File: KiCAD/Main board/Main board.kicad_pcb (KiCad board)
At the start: 2 copper layers, 190 x 125 mm, 123 parts, among them J1 Conn_01x03, J10 Conn_01x03, J11 Conn_01x03, J12 Conn_01x03, J2 Conn_01x03, J3 Conn_01x02, J4 Conn_01x02, J5 Conn_01x03, J6 Conn_01x02, J7 Conn_01x03, J8 Conn_01x02, J9 Conn_01x03, U1 PCM1789, U12 LIN_REG_±5V, U13 LIN_REG_±5V, U14 LIN_REG_±12V, U15 LIN_REG_±12V, U18 12V, U19 5V, U2 LM4562, U20 8V, U21 15V, U3 OPA1632DR, U4 OPA1632DR, U5 OPA1632DR, U7 PCM1804, U9 SEPIC_-15V_LT3579

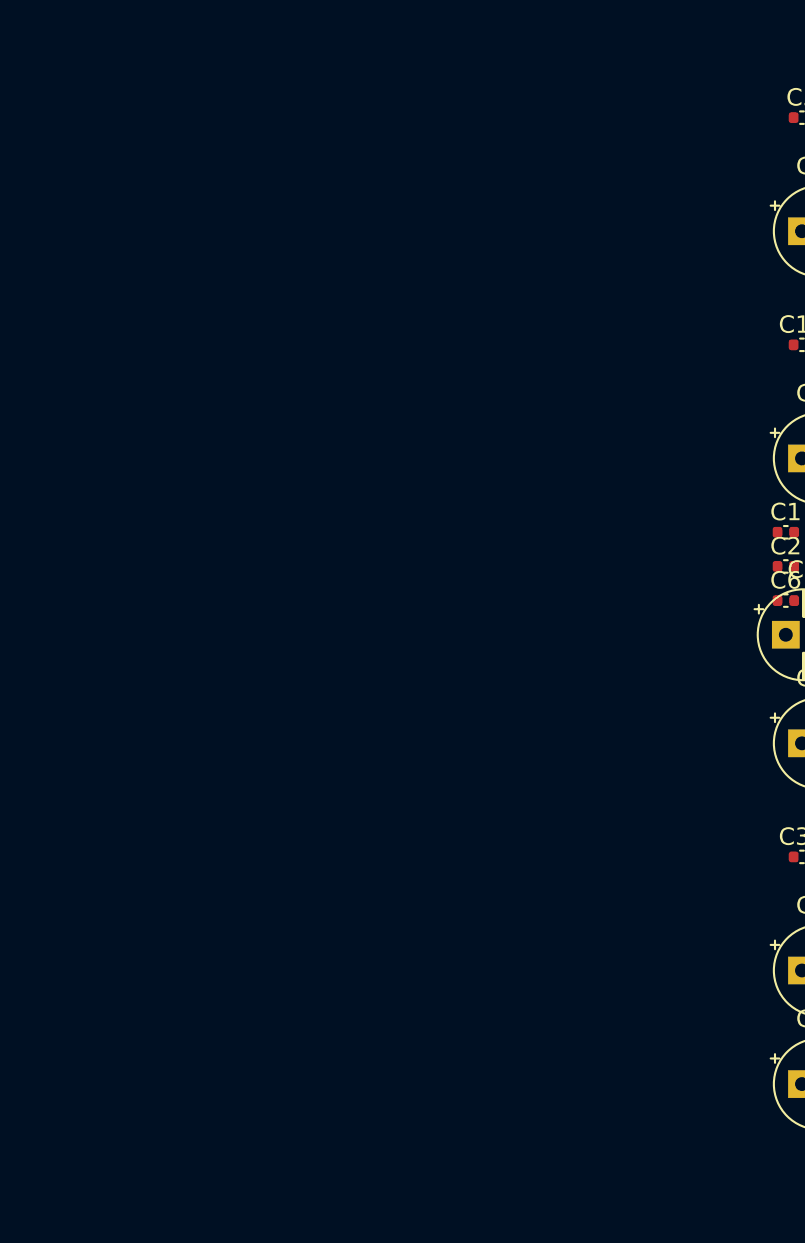
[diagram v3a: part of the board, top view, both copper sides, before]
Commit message: Worked on SDD, main board schematic and LTspice discrete linear regulator
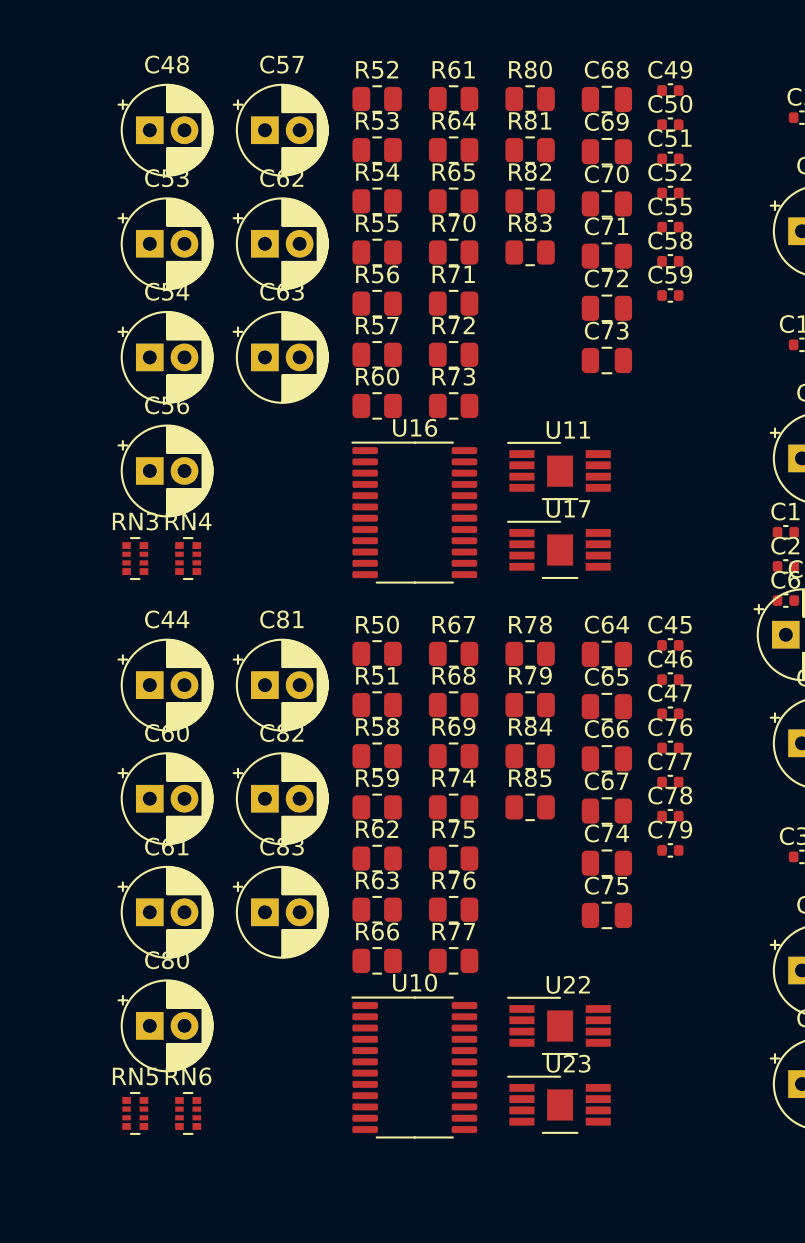
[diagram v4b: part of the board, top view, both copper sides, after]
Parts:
- added C44: 22uF, Capacitor_THT:CP_Radial_D5.0mm_P2.00mm, F.Cu at (278.1, 71.8)
- added C45: 100n, Capacitor_SMD:C_0402_1005Metric, F.Cu at (308.2, 69.5)
- added C46: 100n, Capacitor_SMD:C_0402_1005Metric, F.Cu at (308.2, 71.5)
- added C47: 100n, Capacitor_SMD:C_0402_1005Metric, F.Cu at (308.2, 73.5)
- added C48: 22uF, Capacitor_THT:CP_Radial_D5.0mm_P2.00mm, F.Cu at (278.1, 39.8)
- added C49: 100n, Capacitor_SMD:C_0402_1005Metric, F.Cu at (308.2, 37.5)
- added C50: 100n, Capacitor_SMD:C_0402_1005Metric, F.Cu at (308.2, 39.5)
- added C51: 100n, Capacitor_SMD:C_0402_1005Metric, F.Cu at (308.2, 41.5)
- added C52: 100n, Capacitor_SMD:C_0402_1005Metric, F.Cu at (308.2, 43.4)
- added C53: 22uF, Capacitor_THT:CP_Radial_D5.0mm_P2.00mm, F.Cu at (278.1, 46.4)
- added C54: 22uF, Capacitor_THT:CP_Radial_D5.0mm_P2.00mm, F.Cu at (278.1, 52.9)
- added C55: 100n, Capacitor_SMD:C_0402_1005Metric, F.Cu at (308.2, 45.4)
- added C56: 22uF, Capacitor_THT:CP_Radial_D5.0mm_P2.00mm, F.Cu at (278.1, 59.5)
- added C57: 22uF, Capacitor_THT:CP_Radial_D5.0mm_P2.00mm, F.Cu at (284.8, 39.8)
- added C58: 100n, Capacitor_SMD:C_0402_1005Metric, F.Cu at (308.2, 47.4)
- added C59: 100n, Capacitor_SMD:C_0402_1005Metric, F.Cu at (308.2, 49.4)
- added C60: 22uF, Capacitor_THT:CP_Radial_D5.0mm_P2.00mm, F.Cu at (278.1, 78.4)
- added C61: 22uF, Capacitor_THT:CP_Radial_D5.0mm_P2.00mm, F.Cu at (278.1, 84.9)
- added C62: 22uF, Capacitor_THT:CP_Radial_D5.0mm_P2.00mm, F.Cu at (284.8, 46.4)
- added C63: 22uF, Capacitor_THT:CP_Radial_D5.0mm_P2.00mm, F.Cu at (284.8, 52.9)
- added C64: 680p, Capacitor_SMD:C_0805_2012Metric, F.Cu at (304.5, 70.1)
- added C65: 680, Capacitor_SMD:C_0805_2012Metric, F.Cu at (304.5, 73.1)
- added C66: 680p, Capacitor_SMD:C_0805_2012Metric, F.Cu at (304.5, 76.1)
- added C67: 680, Capacitor_SMD:C_0805_2012Metric, F.Cu at (304.5, 79.1)
- added C68: 680p, Capacitor_SMD:C_0805_2012Metric, F.Cu at (304.5, 38.1)
- added C69: 680, Capacitor_SMD:C_0805_2012Metric, F.Cu at (304.5, 41.1)
- added C70: 680p, Capacitor_SMD:C_0805_2012Metric, F.Cu at (304.5, 44.1)
- added C71: 680, Capacitor_SMD:C_0805_2012Metric, F.Cu at (304.5, 47.1)
- added C72: 2n2, Capacitor_SMD:C_0805_2012Metric, F.Cu at (304.5, 50.1)
- added C73: 2n2, Capacitor_SMD:C_0805_2012Metric, F.Cu at (304.5, 53.1)
- added C74: 2n2, Capacitor_SMD:C_0805_2012Metric, F.Cu at (304.5, 82.1)
- added C75: 2n2, Capacitor_SMD:C_0805_2012Metric, F.Cu at (304.5, 85.1)
- added C76: 100n, Capacitor_SMD:C_0402_1005Metric, F.Cu at (308.2, 75.4)
- added C77: 100n, Capacitor_SMD:C_0402_1005Metric, F.Cu at (308.2, 77.4)
- added C78: 100n, Capacitor_SMD:C_0402_1005Metric, F.Cu at (308.2, 79.4)
- added C79: 100n, Capacitor_SMD:C_0402_1005Metric, F.Cu at (308.2, 81.4)
- added C80: 22uF, Capacitor_THT:CP_Radial_D5.0mm_P2.00mm, F.Cu at (278.1, 91.5)
- added C81: 22uF, Capacitor_THT:CP_Radial_D5.0mm_P2.00mm, F.Cu at (284.8, 71.8)
- added C82: 22uF, Capacitor_THT:CP_Radial_D5.0mm_P2.00mm, F.Cu at (284.8, 78.4)
- added C83: 22uF, Capacitor_THT:CP_Radial_D5.0mm_P2.00mm, F.Cu at (284.8, 84.9)
- added R50: 10R, Resistor_SMD:R_0805_2012Metric, F.Cu at (291.2, 70.0)
- added R51: 10R, Resistor_SMD:R_0805_2012Metric, F.Cu at (291.2, 73.0)
- added R52: 10R, Resistor_SMD:R_0805_2012Metric, F.Cu at (291.2, 38.0)
- added R53: 10R, Resistor_SMD:R_0805_2012Metric, F.Cu at (291.2, 41.0)
- added R54: 10R, Resistor_SMD:R_0805_2012Metric, F.Cu at (291.2, 43.9)
- added R55: 10R, Resistor_SMD:R_0805_2012Metric, F.Cu at (291.2, 46.9)
- added R56: 10R, Resistor_SMD:R_0805_2012Metric, F.Cu at (291.2, 49.8)
- added R57: 10R, Resistor_SMD:R_0805_2012Metric, F.Cu at (291.2, 52.8)
- added R58: 1k, Resistor_SMD:R_0805_2012Metric, F.Cu at (291.2, 75.9)
- added R59: 1k, Resistor_SMD:R_0805_2012Metric, F.Cu at (291.2, 78.9)
- added R60: 1k, Resistor_SMD:R_0805_2012Metric, F.Cu at (291.2, 55.7)
- added R61: 1k, Resistor_SMD:R_0805_2012Metric, F.Cu at (295.7, 38.0)
- added R62: 1k, Resistor_SMD:R_0805_2012Metric, F.Cu at (291.2, 81.8)
- added R63: 1k, Resistor_SMD:R_0805_2012Metric, F.Cu at (291.2, 84.8)
- added R64: 1k, Resistor_SMD:R_0805_2012Metric, F.Cu at (295.7, 41.0)
- added R65: 1k, Resistor_SMD:R_0805_2012Metric, F.Cu at (295.7, 43.9)
- added R66: 4k7, Resistor_SMD:R_0805_2012Metric, F.Cu at (291.2, 87.7)
- added R67: 4k7, Resistor_SMD:R_0805_2012Metric, F.Cu at (295.7, 70.0)
- added R68: 4k7, Resistor_SMD:R_0805_2012Metric, F.Cu at (295.7, 73.0)
- added R69: 4k7, Resistor_SMD:R_0805_2012Metric, F.Cu at (295.7, 75.9)
- added R70: 4k7, Resistor_SMD:R_0805_2012Metric, F.Cu at (295.7, 46.9)
- added R71: 4k7, Resistor_SMD:R_0805_2012Metric, F.Cu at (295.7, 49.8)
- added R72: 4k7, Resistor_SMD:R_0805_2012Metric, F.Cu at (295.7, 52.8)
- added R73: 4k7, Resistor_SMD:R_0805_2012Metric, F.Cu at (295.7, 55.7)
- added R74: 39, Resistor_SMD:R_0805_2012Metric, F.Cu at (295.7, 78.9)
- added R75: 39, Resistor_SMD:R_0805_2012Metric, F.Cu at (295.7, 81.8)
- added R76: 39, Resistor_SMD:R_0805_2012Metric, F.Cu at (295.7, 84.8)
- added R77: 39, Resistor_SMD:R_0805_2012Metric, F.Cu at (295.7, 87.7)
- added R78: 10R, Resistor_SMD:R_0805_2012Metric, F.Cu at (300.1, 70.0)
- added R79: 10R, Resistor_SMD:R_0805_2012Metric, F.Cu at (300.1, 73.0)
- added R80: 39, Resistor_SMD:R_0805_2012Metric, F.Cu at (300.1, 38.0)
- added R81: 39, Resistor_SMD:R_0805_2012Metric, F.Cu at (300.1, 41.0)
- added R82: 39, Resistor_SMD:R_0805_2012Metric, F.Cu at (300.1, 43.9)
- added R83: 39, Resistor_SMD:R_0805_2012Metric, F.Cu at (300.1, 46.9)
- added R84: 10R, Resistor_SMD:R_0805_2012Metric, F.Cu at (300.1, 75.9)
- added R85: 10R, Resistor_SMD:R_0805_2012Metric, F.Cu at (300.1, 78.9)
- added RN3: 22R, Resistor_SMD:R_Array_Convex_4x0402, F.Cu at (277.3, 64.5)
- added RN4: 22R, Resistor_SMD:R_Array_Convex_4x0402, F.Cu at (280.4, 64.5)
- added RN5: 22R, Resistor_SMD:R_Array_Convex_4x0402, F.Cu at (277.3, 96.5)
- added RN6: 22R, Resistor_SMD:R_Array_Convex_4x0402, F.Cu at (280.4, 96.5)
- added U10: PCM1789, Package_SO:TSSOP-24_4.4x7.8mm_P0.65mm, F.Cu at (293.4, 93.9)
- added U11: OPA1632DR, Audio-DSP:VSSOP-8_3.0x3.0mm_P0.65_TP1.8x1.5, F.Cu at (301.8, 59.5)
- added U16: PCM1789, Package_SO:TSSOP-24_4.4x7.8mm_P0.65mm, F.Cu at (293.4, 61.9)
- added U17: OPA1632DR, Audio-DSP:VSSOP-8_3.0x3.0mm_P0.65_TP1.8x1.5, F.Cu at (301.8, 64.0)
- added U22: OPA1632DR, Audio-DSP:VSSOP-8_3.0x3.0mm_P0.65_TP1.8x1.5, F.Cu at (301.8, 91.5)
- added U23: OPA1632DR, Audio-DSP:VSSOP-8_3.0x3.0mm_P0.65_TP1.8x1.5, F.Cu at (301.8, 96.0)

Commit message: Worked on main board schematic and PCB, added symbols to symbol library
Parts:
- added C100: 100n, Capacitor_SMD:C_0402_1005Metric, F.Cu at (316.1, 59.1)
- added C101: 100n, Capacitor_SMD:C_0402_1005Metric, F.Cu at (319.0, 53.2)
- added C102: 22uF, Capacitor_THT:CP_Radial_D5.0mm_P2.00mm, F.Cu at (291.8, 54.5)
- added C103: 22uF, Capacitor_THT:CP_Radial_D5.0mm_P2.00mm, F.Cu at (291.8, 61.0)
- added C104: 100n, Capacitor_SMD:C_0402_1005Metric, F.Cu at (319.0, 55.2)
- added C105: 3n3, Capacitor_SMD:C_0805_2012Metric, F.Cu at (298.3, 45.1)
- added C106: 1n, Capacitor_SMD:C_0805_2012Metric, F.Cu at (298.3, 48.1)
- added C107: 1n, Capacitor_SMD:C_0805_2012Metric, F.Cu at (298.3, 51.1)
- added C108: 2n7, Capacitor_SMD:C_0805_2012Metric, F.Cu at (298.3, 54.1)
- added C109: 100n, Capacitor_SMD:C_0402_1005Metric, F.Cu at (319.0, 57.1)
- added C110: 100n, Capacitor_SMD:C_0402_1005Metric, F.Cu at (331.9, 56.1)
- added C111: 100n, Capacitor_SMD:C_0402_1005Metric, F.Cu at (319.0, 59.1)
- added C112: 1u, Capacitor_SMD:C_0402_1005Metric, F.Cu at (296.4, 126.1)
- added C113: 1u, Capacitor_SMD:C_0402_1005Metric, F.Cu at (296.4, 128.1)
- added C114: 1u, Capacitor_SMD:C_0402_1005Metric, F.Cu at (296.4, 130.0)
- added C115: 3n3, Capacitor_SMD:C_0805_2012Metric, F.Cu at (346.7, 52.4)
- added C116: 3n3, Capacitor_SMD:C_0805_2012Metric, F.Cu at (346.7, 55.4)
- added C117: 1n, Capacitor_SMD:C_0805_2012Metric, F.Cu at (346.7, 58.4)
- added C118: 1n, Capacitor_SMD:C_0805_2012Metric, F.Cu at (346.7, 61.5)
- added C119: 2n7, Capacitor_SMD:C_0805_2012Metric, F.Cu at (346.7, 64.5)
- added C120: 100n, Capacitor_SMD:C_0402_1005Metric, F.Cu at (331.9, 58.1)
- added C35: 1n, Capacitor_SMD:C_0805_2012Metric, F.Cu at (298.3, 33.1)
- added C40: 1n, Capacitor_SMD:C_0805_2012Metric, F.Cu at (298.3, 36.1)
- added C84: 100n, Capacitor_SMD:C_0402_1005Metric, F.Cu at (313.2, 55.2)
- added C85: 1u, Capacitor_SMD:C_0402_1005Metric, F.Cu at (296.4, 124.1)
- added C86: 100n, Capacitor_SMD:C_0402_1005Metric, F.Cu at (313.2, 57.1)
- added C87: 100n, Capacitor_SMD:C_0402_1005Metric, F.Cu at (313.2, 59.1)
- added C88: 100n, Capacitor_SMD:C_0402_1005Metric, F.Cu at (316.1, 53.2)
- added C89: 22uF, Capacitor_THT:CP_Radial_D5.0mm_P2.00mm, F.Cu at (291.8, 34.8)
- added C90: 3n3, Capacitor_SMD:C_0805_2012Metric, F.Cu at (298.3, 42.1)
- added C91: 100n, Capacitor_SMD:C_0402_1005Metric, F.Cu at (316.1, 55.2)
- added C92: 3n3, Capacitor_SMD:C_0805_2012Metric, F.Cu at (342.3, 52.4)
- added C93: 3n3, Capacitor_SMD:C_0805_2012Metric, F.Cu at (342.3, 55.4)
- added C94: 1n, Capacitor_SMD:C_0805_2012Metric, F.Cu at (342.3, 58.4)
- added C95: 1n, Capacitor_SMD:C_0805_2012Metric, F.Cu at (342.3, 61.5)
- added C96: 2n7, Capacitor_SMD:C_0805_2012Metric, F.Cu at (342.3, 64.5)
- added C97: 100n, Capacitor_SMD:C_0402_1005Metric, F.Cu at (316.1, 57.1)
- added C98: 22uF, Capacitor_THT:CP_Radial_D5.0mm_P2.00mm, F.Cu at (291.8, 41.4)
- added C99: 22uF, Capacitor_THT:CP_Radial_D5.0mm_P2.00mm, F.Cu at (291.8, 47.9)
- added J13: Conn_01x02, Connector_Phoenix_MC:PhoenixContact_MCV_1,5_2-G-3.5_1x02_P3.50mm_Vertical, F.Cu at (150.4, 193.3)
- added J14: Conn_01x02, Connector_Phoenix_MC:PhoenixContact_MCV_1,5_2-G-3.5_1x02_P3.50mm_Vertical, F.Cu at (150.4, 207.3)
- added J15: Conn_01x02, Connector_Phoenix_MC:PhoenixContact_MCV_1,5_2-G-3.5_1x02_P3.50mm_Vertical, F.Cu at (310.3, 112.0)
- added NT3: NetTie_2, Audio-DSP:NetTie-2_SMD_Pad0.3mm, F.Cu at (317.9, 64.4)
- added NT4: NetTie_2, Audio-DSP:NetTie-2_SMD_Pad0.3mm, F.Cu at (317.9, 65.9)
- added R100: 39, Resistor_SMD:R_0805_2012Metric, F.Cu at (329.0, 47.8)
- added R101: 39, Resistor_SMD:R_0805_2012Metric, F.Cu at (329.0, 50.7)
- added R102: 10R, Resistor_SMD:R_0805_2012Metric, F.Cu at (311.5, 38.9)
- added R103: 1k, Resistor_SMD:R_0805_2012Metric, F.Cu at (311.5, 41.9)
- added R104: 47k, Resistor_SMD:R_0805_2012Metric, F.Cu at (311.5, 44.8)
- added R105: 220, Resistor_SMD:R_0805_2012Metric, F.Cu at (311.5, 47.8)
- added R106: 1k, Resistor_SMD:R_0805_2012Metric, F.Cu at (311.5, 50.7)
- added R107: 1k, Resistor_SMD:R_0805_2012Metric, F.Cu at (315.9, 33.0)
- added R108: 270, Resistor_SMD:R_0805_2012Metric, F.Cu at (315.9, 36.0)
- added R109: 270, Resistor_SMD:R_0805_2012Metric, F.Cu at (315.9, 38.9)
- added R110: 39, Resistor_SMD:R_0805_2012Metric, F.Cu at (315.9, 41.9)
- added R111: 39, Resistor_SMD:R_0805_2012Metric, F.Cu at (315.9, 44.8)
- added R112: 1k, Resistor_SMD:R_0805_2012Metric, F.Cu at (315.9, 47.8)
- added R113: 1k, Resistor_SMD:R_0805_2012Metric, F.Cu at (329.0, 53.7)
- added R114: 220, Resistor_SMD:R_0805_2012Metric, F.Cu at (333.4, 33.0)
- added R115: 2M2, Resistor_SMD:R_0805_2012Metric, F.Cu at (333.4, 36.0)
- added R116: 1k, Resistor_SMD:R_0805_2012Metric, F.Cu at (333.4, 38.9)
- added R117: 0, Resistor_SMD:R_0805_2012Metric, F.Cu at (333.4, 41.9)
- added R118: 0, Resistor_SMD:R_0805_2012Metric, F.Cu at (333.4, 44.8)
- added R119: 1k, Resistor_SMD:R_0805_2012Metric, F.Cu at (333.4, 47.8)
- added R120: 1k, Resistor_SMD:R_0805_2012Metric, F.Cu at (333.4, 50.7)
- added R121: 270, Resistor_SMD:R_0805_2012Metric, F.Cu at (333.4, 53.7)
- added R122: 270, Resistor_SMD:R_0805_2012Metric, F.Cu at (337.9, 33.0)
- added R123: 39, Resistor_SMD:R_0805_2012Metric, F.Cu at (337.9, 36.0)
- added R124: 39, Resistor_SMD:R_0805_2012Metric, F.Cu at (337.9, 38.9)
- added R125: 1k, Resistor_SMD:R_0805_2012Metric, F.Cu at (337.9, 41.9)
- added R37: 1k, Resistor_SMD:R_0805_2012Metric, F.Cu at (302.7, 38.9)
- added R40: 1k, Resistor_SMD:R_0805_2012Metric, F.Cu at (302.7, 47.8)
- added R41: 270, Resistor_SMD:R_0805_2012Metric, F.Cu at (302.7, 50.7)
- added R44: 39, Resistor_SMD:R_0805_2012Metric, F.Cu at (307.1, 38.9)
- added R45: 47k, Resistor_SMD:R_0805_2012Metric, F.Cu at (324.6, 33.0)
- added R48: 10R, Resistor_SMD:R_0805_2012Metric, F.Cu at (307.1, 44.8)
- added R49: 220, Resistor_SMD:R_0805_2012Metric, F.Cu at (307.1, 47.8)
- added R86: 47k, Resistor_SMD:R_0805_2012Metric, F.Cu at (307.1, 50.7)
- added R87: 10R, Resistor_SMD:R_0805_2012Metric, F.Cu at (311.5, 33.0)
- added R88: 10R, Resistor_SMD:R_0805_2012Metric, F.Cu at (311.5, 36.0)
- added R89: 47k, Resistor_SMD:R_0805_2012Metric, F.Cu at (324.6, 38.9)
- added R90: 47k, Resistor_SMD:R_0805_2012Metric, F.Cu at (324.6, 41.9)
- added R91: 220, Resistor_SMD:R_0805_2012Metric, F.Cu at (324.6, 44.8)
- added R92: 2M2, Resistor_SMD:R_0805_2012Metric, F.Cu at (324.6, 47.8)
- added R93: 1k, Resistor_SMD:R_0805_2012Metric, F.Cu at (324.6, 50.7)
- added R94: 0, Resistor_SMD:R_0805_2012Metric, F.Cu at (324.6, 53.7)
- added R95: 0, Resistor_SMD:R_0805_2012Metric, F.Cu at (329.0, 33.0)
- added R96: 1k, Resistor_SMD:R_0805_2012Metric, F.Cu at (329.0, 36.0)
- added R97: 1k, Resistor_SMD:R_0805_2012Metric, F.Cu at (329.0, 38.9)
- added R98: 270, Resistor_SMD:R_0805_2012Metric, F.Cu at (329.0, 41.9)
- added R99: 270, Resistor_SMD:R_0805_2012Metric, F.Cu at (329.0, 44.8)
- added RN7: 22R, Resistor_SMD:R_Array_Convex_4x0402, F.Cu at (318.5, 61.9)
- added TP1: TestPoint, TestPoint:TestPoint_Pad_D2.0mm, F.Cu at (284.8, 108.7)
- added TP10: TestPoint, TestPoint:TestPoint_Pad_D2.0mm, F.Cu at (288.9, 124.9)
- added TP11: TestPoint, TestPoint:TestPoint_Pad_D2.0mm, F.Cu at (292.9, 108.7)
- added TP12: TestPoint, TestPoint:TestPoint_Pad_D2.0mm, F.Cu at (292.9, 112.7)
- added TP13: TestPoint, TestPoint:TestPoint_Pad_D2.0mm, F.Cu at (292.9, 116.8)
- added TP14: TestPoint, TestPoint:TestPoint_Pad_D2.0mm, F.Cu at (292.9, 120.8)
- added TP2: TestPoint, TestPoint:TestPoint_Pad_D2.0mm, F.Cu at (284.8, 112.7)
- added TP3: TestPoint, TestPoint:TestPoint_Pad_D2.0mm, F.Cu at (284.8, 116.8)
- added TP4: TestPoint, TestPoint:TestPoint_Pad_D2.0mm, F.Cu at (284.8, 120.8)
- added TP5: TestPoint, TestPoint:TestPoint_Pad_D2.0mm, F.Cu at (284.8, 124.9)
- added TP6: TestPoint, TestPoint:TestPoint_Pad_D2.0mm, F.Cu at (288.9, 108.7)
- added TP7: TestPoint, TestPoint:TestPoint_Pad_D2.0mm, F.Cu at (288.9, 112.7)
- added TP8: TestPoint, TestPoint:TestPoint_Pad_D2.0mm, F.Cu at (288.9, 116.8)
- added TP9: TestPoint, TestPoint:TestPoint_Pad_D2.0mm, F.Cu at (288.9, 120.8)
- added U24: LM4562, Package_SO:SOIC-8_3.9x4.9mm_P1.27mm, F.Cu at (304.7, 61.9)
- added U25: OPA1632DR, Audio-DSP:VSSOP-8_3.0x3.0mm_P0.65_TP1.8x1.5, F.Cu at (312.9, 66.9)
- added U26: LM4562, Package_SO:SOIC-8_3.9x4.9mm_P1.27mm, F.Cu at (344.3, 34.8)
- added U27: OPA1632DR, Audio-DSP:VSSOP-8_3.0x3.0mm_P0.65_TP1.8x1.5, F.Cu at (326.4, 57.5)
- added U28: 12V, Audio-DSP:BUCK_MAX17634C_xxV, F.Cu at (163.0, 207.5)
- added U29: AP2111H-3.3TRG1, Package_TO_SOT_SMD:SOT-223, F.Cu at (299.9, 110.8)
- added U30: LM4562, Package_SO:SOIC-8_3.9x4.9mm_P1.27mm, F.Cu at (344.3, 41.2)
- added U31: AP2111H-3.3TRG1, Package_TO_SOT_SMD:SOT-223, F.Cu at (299.9, 119.0)
- added U32: LM4562, Package_SO:SOIC-8_3.9x4.9mm_P1.27mm, F.Cu at (344.3, 47.7)
- added U33: OPA1632DR, Audio-DSP:VSSOP-8_3.0x3.0mm_P0.65_TP1.8x1.5, F.Cu at (326.4, 62.0)
- added U6: LM4562, Package_SO:SOIC-8_3.9x4.9mm_P1.27mm, F.Cu at (304.7, 55.4)
- C41: value 1n -> 2n7
- C42: value 1n -> 22uF; footprint Capacitor_SMD:C_0805_2012Metric -> Capacitor_THT:CP_Radial_D5.0mm_P2.00mm
- C43: value 2.7n -> 100n; footprint Capacitor_SMD:C_0805_2012Metric -> Capacitor_SMD:C_0402_1005Metric
- R42: value 1k -> 270
- R43: value 2.7k -> 39
- R46: value 39 -> 47k
- R47: value 39 -> 10R
- R5, R50, R51, R54, R57, R8: value 10R -> 4R7
- moved C14 66.4 mm to (285.1, 94.1)
- moved C5 62.2 mm to (301.9, 99.7)
- moved C31 56.7 mm to (285.1, 34.8)
- moved C44 56.3 mm to (322.5, 106.5)
- moved C48 56.3 mm to (322.5, 74.5)
- moved C53 56.3 mm to (322.5, 81.0)
- moved C54 56.3 mm to (322.5, 87.6)
- moved C56 56.3 mm to (322.5, 94.1)
- moved C57 56.3 mm to (329.1, 74.5)
- moved C60 56.3 mm to (322.5, 113.0)
- moved C61 56.3 mm to (322.5, 119.6)
- moved C62 56.3 mm to (329.1, 81.0)
- moved C63 56.3 mm to (329.1, 87.6)
- moved C64 56.3 mm to (348.9, 104.7)
- moved C65 56.3 mm to (348.9, 107.7)
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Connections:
- net /DAC_CH1_2/AMUTEI_CH1_2 renamed /DAC_CH1_2/AMUTEI_DAC_CH1_2
- net /DAC_CH1_2/BCK_CH1_2 renamed /DAC_CH1_2/BCK_DAC_CH1_2
- net /DAC_CH1_2/DIN_CH1_2 renamed /DAC_CH1_2/DIN_DAC_CH1_2
- net /DAC_CH1_2/LRCK_CH1_2 renamed /DAC_CH1_2/LRCK_DAC_CH1_2
- net /DAC_CH1_2/SCKI_CH1_2 renamed /DAC_CH1_2/SCKI_DAC_CH1_2
- net /DAC_CH1_2/SCL_CH1_2 renamed /DAC_CH1_2/SCL_DAC_CH1_2
- net /DAC_CH1_2/SDA_CH1_2 renamed /DAC_CH1_2/SDA_DAC_CH1_2
- net /DAC_CH1_2/VOUT_CH1(+) renamed /DAC_CH1_2/VOUT_XLR_CH1(+)
- net /DAC_CH1_2/VOUT_CH1(-) renamed /DAC_CH1_2/VOUT_XLR_CH1(-)
- net /DAC_CH1_2/VOUT_CH2(+) renamed /DAC_CH1_2/VOUT_XLR_CH2(+)
- net /DAC_CH1_2/VOUT_CH2(-) renamed /DAC_CH1_2/VOUT_XLR_CH2(-)
- net /DAC_CH3_4/AMUTEI_CH1_2 renamed /DAC_CH3_4/AMUTEI_DAC_CH3_4
- net /DAC_CH3_4/BCK_CH1_2 renamed /DAC_CH3_4/BCK_DAC_CH3_4
- net /DAC_CH3_4/DIN_CH1_2 renamed /DAC_CH3_4/DIN_DAC_CH3_4
- net /DAC_CH3_4/LRCK_CH1_2 renamed /DAC_CH3_4/LRCK_DAC_CH3_4
- net /DAC_CH3_4/SCKI_CH1_2 renamed /DAC_CH3_4/SCKI_DAC_CH3_4
- net /DAC_CH3_4/SCL_CH1_2 renamed /DAC_CH3_4/SCL_DAC_CH3_4
- net /DAC_CH3_4/SDA_CH1_2 renamed /DAC_CH3_4/SDA_DAC_CH3_4
- net /DAC_CH5_6/AMUTEI_CH1_2 renamed /DAC_CH5_6/AMUTEI_DAC_CH5_6
- net /DAC_CH5_6/BCK_CH1_2 renamed /DAC_CH5_6/BCK_DAC_CH5_6
- net /DAC_CH5_6/DIN_CH1_2 renamed /DAC_CH5_6/DIN_DAC_CH5_6
- net /DAC_CH5_6/LRCK_CH1_2 renamed /DAC_CH5_6/LRCK_DAC_CH5_6
- net /DAC_CH5_6/SCKI_CH1_2 renamed /DAC_CH5_6/SCKI_DAC_CH5_6
- net /DAC_CH5_6/SCL_CH1_2 renamed /DAC_CH5_6/SCL_DAC_CH5_6
- net /DAC_CH5_6/SDA_CH1_2 renamed /DAC_CH5_6/SDA_DAC_CH5_6
- net Net-(U18-VIN) renamed /POWER_SUPPLIES/DC_POWER_IN
- C39 pad 1: +3.3V -> +3V3D2
- C41 pad 1: Net-(U5A-VIN+) -> Net-(U7-VINL+)
- C41 pad 2: Net-(U5A-VOUT-) -> Net-(U7-VINL-)
- C42 pad 1: Net-(U5A-VIN-) -> +3V3D1
- C42 pad 2: Net-(U5A-VOUT+) -> GND
- C43 pad 1: Net-(C43-Pad1) -> GND
- C43 pad 2: Net-(C43-Pad2) -> +3V3D1
- C44 pad 1: +3.3V -> +3V3D2
- C45 pad 1: +3.3V -> +3V3D2
- C48 pad 1: +3.3V -> +3V3D2
- C49 pad 1: +3.3V -> +3V3D2
- C5 pad 1: +3.3V -> +3V3D2
- C72 pad 1: /DAC_CH3_4/VOUT_CH1(-) -> /DAC_CH3_4/VOUT_XLR_CH3(-)
- C72 pad 2: /DAC_CH3_4/VOUT_CH1(+) -> /DAC_CH3_4/VOUT_XLR_CH3(+)
- C73 pad 1: /DAC_CH3_4/VOUT_CH2(-) -> /DAC_CH3_4/VOUT_XLR_CH4(-)
- C73 pad 2: /DAC_CH3_4/VOUT_CH2(+) -> /DAC_CH3_4/VOUT_XLR_CH4(+)
- C74 pad 1: /DAC_CH5_6/VOUT_CH1(-) -> /DAC_CH5_6/VOUT_XLR_CH5(-)
- C74 pad 2: /DAC_CH5_6/VOUT_CH1(+) -> /DAC_CH5_6/VOUT_XLR_CH5(+)
- C75 pad 1: /DAC_CH5_6/VOUT_CH2(-) -> /DAC_CH5_6/VOUT_XLR_CH6(-)
- C75 pad 2: /DAC_CH5_6/VOUT_CH2(+) -> /DAC_CH5_6/VOUT_XLR_CH6(+)
- H3 pad 1: unconnected-(H3-Pad1) -> GND
- J1 pad 1: unconnected-(J1-Pin_1-Pad1) -> /ADC_CH3_4/XLR_CH3(+)
- J1 pad 2: unconnected-(J1-Pin_2-Pad2) -> GND
- J1 pad 3: unconnected-(J1-Pin_3-Pad3) -> /ADC_CH3_4/XLR_CH3(-)
- J10 pad 1: /VOUT CH1(-) -> /DAC_CH3_4/VOUT_XLR_CH4(+)
- J10 pad 3: /VOUT CH1(+) -> /DAC_CH3_4/VOUT_XLR_CH4(-)
- J11 pad 1: /VOUT CH5(-) -> /DAC_CH5_6/VOUT_XLR_CH5(+)
- J11 pad 3: /VOUT CH5(+) -> /DAC_CH5_6/VOUT_XLR_CH5(-)
- J12 pad 1: /VOUT CH6(-) -> /DAC_CH5_6/VOUT_XLR_CH6(+)
- J12 pad 3: /VOUT CH6(+) -> /DAC_CH5_6/VOUT_XLR_CH6(-)
- J2 pad 2: unconnected-(J2-Pin_2-Pad2) -> GND
- J3 pad 1: unconnected-(J3-Pin_1-Pad1) -> /ADC_CH1_2/RCA_JACK_CH1(+)
- J3 pad 2: unconnected-(J3-Pin_2-Pad2) -> /ADC_CH1_2/RCA_JACK_CH1(REF)
- J4 pad 1: unconnected-(J4-Pin_1-Pad1) -> /ADC_CH1_2/RCA_JACK_CH2(+)
- J4 pad 2: unconnected-(J4-Pin_2-Pad2) -> /ADC_CH1_2/RCA_JACK_CH2(REF)
- J9 pad 1: /VOUT CH2(-) -> /DAC_CH3_4/VOUT_XLR_CH3(+)
- J9 pad 3: /VOUT CH2(+) -> /DAC_CH3_4/VOUT_XLR_CH3(-)
- R1 pad 1: +12V -> +12VA2
- R2 pad 2: -12V -> -12VA2
- R3 pad 1: +12V -> +12VA2
- R35 pad 1: +12V -> +12VA1
- R36 pad 2: -12V -> -12VA1
- R38 pad 1: +12V -> +12VA1
- R39 pad 2: -12V -> -12VA1
- R4 pad 2: -12V -> -12VA2
- R42 pad 1: Net-(U6A--) -> Net-(U5A-VIN-)
- R42 pad 2: Net-(U5A-VIN+) -> Net-(U7-VINL-)
- R43 pad 1: Net-(U5A-VIN+) -> Net-(U5A-VOUT-)
- R43 pad 2: Net-(C43-Pad1) -> Net-(U7-VINL+)
- R46 pad 1: Net-(U5A-VOUT-) -> Net-(R115-Pad1)
- R46 pad 2: Net-(C43-Pad1) -> /ADC_CH3_4/XLR_CH4(-)
- R47 pad 1: Net-(U5A-VOUT+) -> +12VA1
- R47 pad 2: Net-(C43-Pad2) -> Net-(U24C-V+)
- R5 pad 1: +5V -> +5VA2
- R50 pad 1: +5V -> +5VA2
- R51 pad 1: +5V -> +5VA2
- R52 pad 1: +12V -> +12VA2
- R53 pad 2: -12V -> -12VA2
- R54 pad 1: +5V -> +5VA2
- R55 pad 1: +12V -> +12VA2
- R56 pad 2: -12V -> -12VA2
- R57 pad 1: +5V -> +5VA2
- R6 pad 1: +12V -> +12VA2
- R66 pad 2: /DAC_CH5_6/VOUT_CH1(+) -> /DAC_CH5_6/VOUT_XLR_CH5(+)
- R67 pad 2: /DAC_CH5_6/VOUT_CH1(-) -> /DAC_CH5_6/VOUT_XLR_CH5(-)
- R68 pad 2: /DAC_CH5_6/VOUT_CH2(-) -> /DAC_CH5_6/VOUT_XLR_CH6(-)
- R69 pad 2: /DAC_CH5_6/VOUT_CH2(+) -> /DAC_CH5_6/VOUT_XLR_CH6(+)
- R7 pad 2: -12V -> -12VA2
- R70 pad 2: /DAC_CH3_4/VOUT_CH1(+) -> /DAC_CH3_4/VOUT_XLR_CH3(+)
- R71 pad 2: /DAC_CH3_4/VOUT_CH1(-) -> /DAC_CH3_4/VOUT_XLR_CH3(-)
- R72 pad 2: /DAC_CH3_4/VOUT_CH2(-) -> /DAC_CH3_4/VOUT_XLR_CH4(-)
- R73 pad 2: /DAC_CH3_4/VOUT_CH2(+) -> /DAC_CH3_4/VOUT_XLR_CH4(+)
- R74 pad 2: /DAC_CH5_6/VOUT_CH1(-) -> /DAC_CH5_6/VOUT_XLR_CH5(-)
- R75 pad 2: /DAC_CH5_6/VOUT_CH1(+) -> /DAC_CH5_6/VOUT_XLR_CH5(+)
- R76 pad 2: /DAC_CH5_6/VOUT_CH2(-) -> /DAC_CH5_6/VOUT_XLR_CH6(-)
- R77 pad 2: /DAC_CH5_6/VOUT_CH2(+) -> /DAC_CH5_6/VOUT_XLR_CH6(+)
- R78 pad 1: +12V -> +12VA2
- R79 pad 2: -12V -> -12VA2
- R8 pad 1: +5V -> +5VA2
- R80 pad 2: /DAC_CH3_4/VOUT_CH1(-) -> /DAC_CH3_4/VOUT_XLR_CH3(-)
- R81 pad 2: /DAC_CH3_4/VOUT_CH1(+) -> /DAC_CH3_4/VOUT_XLR_CH3(+)
- R82 pad 2: /DAC_CH3_4/VOUT_CH2(-) -> /DAC_CH3_4/VOUT_XLR_CH4(-)
- R83 pad 2: /DAC_CH3_4/VOUT_CH2(+) -> /DAC_CH3_4/VOUT_XLR_CH4(+)
- R84 pad 1: +12V -> +12VA2
- R85 pad 2: -12V -> -12VA2
- U1 pad 6: +3.3V -> +3V3D2
- U10 pad 24: GND -> +3.3V
- U10 pad 6: +3.3V -> +3V3D2
- U12 pad 1: unconnected-(U12-+8V-Pad1) -> Net-(U12-+8V)
- U12 pad 3: unconnected-(U12-+5V-Pad3) -> +5VA1
- U13 pad 1: unconnected-(U13-+8V-Pad1) -> Net-(U12-+8V)
- U13 pad 3: unconnected-(U13-+5V-Pad3) -> +5VA2
- U14 pad 1: unconnected-(U14-+15V-Pad1) -> Net-(U14-+15V)
- U14 pad 3: +12VA -> +12VA1
- U14 pad 4: unconnected-(U14--12V-Pad4) -> -12VA1
- U14 pad 6: unconnected-(U14--15V-Pad6) -> Net-(U14--15V)
- U15 pad 1: unconnected-(U15-+15V-Pad1) -> Net-(U14-+15V)
- U15 pad 3: unconnected-(U15-+12V-Pad3) -> +12VA2
- U15 pad 4: unconnected-(U15--12V-Pad4) -> -12VA2
- U15 pad 6: unconnected-(U15--15V-Pad6) -> Net-(U14--15V)
- U16 pad 23: GND -> +3.3V
- U16 pad 6: +3.3V -> +3V3D2
- U18 pad 1: unconnected-(U18-VOUT-Pad1) -> Net-(U18-VOUT)
- U19 pad 1: unconnected-(U19-VOUT-Pad1) -> /POWER_SUPPLIES/UI_POWER
- U20 pad 1: unconnected-(U20-VOUT-Pad1) -> Net-(U12-+8V)
- U21 pad 1: unconnected-(U21-VOUT-Pad1) -> Net-(U14-+15V)
- U7 pad 1: unconnected-(U7-VREFL-Pad1) -> Net-(U7-VREFL)
- U7 pad 13: unconnected-(U7-DGND-Pad13) -> GND
- U7 pad 14: unconnected-(U7-VDD-Pad14) -> +3V3D1
- U7 pad 15: unconnected-(U7-DATA/DSDR-Pad15) -> Net-(RN7-R4.1)
- U7 pad 16: unconnected-(U7-BCK/DSDL-Pad16) -> Net-(RN7-R3.1)
- U7 pad 17: unconnected-(U7-LRCK/DSDBCK-Pad17) -> Net-(RN7-R2.1)
- U7 pad 18: unconnected-(U7-SCKI-Pad18) -> Net-(RN7-R1.1)
- U7 pad 2: unconnected-(U7-AGNDL-Pad2) -> GND
- U7 pad 22: unconnected-(U7-VCC-Pad22) -> Net-(U7-VCC)
- U7 pad 23: unconnected-(U7-AGND-Pad23) -> GND
- U7 pad 24: unconnected-(U7-VINR--Pad24) -> Net-(U7-VINR-)
- U7 pad 25: unconnected-(U7-VINR+-Pad25) -> Net-(U7-VINR+)
- U7 pad 26: unconnected-(U7-VCOMR-Pad26) -> Net-(U7-VCOMR)
- U7 pad 27: unconnected-(U7-AGNDR-Pad27) -> GND
- U7 pad 28: unconnected-(U7-VREFR-Pad28) -> Net-(U7-VREFR)
- U7 pad 3: unconnected-(U7-VCOML-Pad3) -> Net-(U7-VCOML)
- U7 pad 4: unconnected-(U7-VINL+-Pad4) -> Net-(U7-VINL+)
- U7 pad 5: unconnected-(U7-VINL--Pad5) -> Net-(U7-VINL-)
- U9 pad 1: unconnected-(U9-VIN-Pad1) -> Net-(U18-VOUT)
- U9 pad 2: unconnected-(U9-GND-Pad2) -> GND
- U9 pad 3: unconnected-(U9-VOUT-Pad3) -> Net-(U14--15V)
- U9 pad 4: unconnected-(U9-GND-Pad4) -> GND
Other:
- board text added: "+12VD1"
- board text added: "+15VD"
- board text added: "+DC IN"
- board text added: "-15VD"
- board text added: "Update stackup and constrain manager from existing design"
- board text removed: "+15V"
- board text removed: "GPIO 0"
- board text removed: "GPIO 1"
- board text removed: "Update stackup and constrain manager"

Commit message: Worked on main board design
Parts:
- added C121: 100n, Capacitor_SMD:C_0402_1005Metric, F.Cu at (342.3, 53.6)
- added C122: 100n, Capacitor_SMD:C_0402_1005Metric, F.Cu at (342.3, 55.6)
- added C123: 100n, Capacitor_SMD:C_0402_1005Metric, F.Cu at (342.3, 57.6)
- added C124: 100n, Capacitor_SMD:C_0402_1005Metric, F.Cu at (342.3, 59.6)
- added D1: 1N4148WS, Diode_SMD:D_SOD-323, B.Cu at (82.0, 63.0)
- added D2: 1N4148WS, Diode_SMD:D_SOD-323, B.Cu at (88.0, 67.0)
- added D3: STS321050B100, Diode_SMD:D_SOD-323, F.Cu at (53.0, 86.0)
- added D4: D_TVS, Diode_SMD:D_SOD-323, F.Cu at (53.0, 92.0)
- added J16: Conn_01x02, Connector_JST:JST_PH_B2B-PH-K_1x02_P2.00mm_Vertical, F.Cu at (71.0, 86.0)
- added J17: Conn_01x02, Connector_JST:JST_PH_B2B-PH-K_1x02_P2.00mm_Vertical, F.Cu at (71.0, 92.5)
- added K1: EA2-12NU, Audio-DSP:EA2-12NU, F.Cu at (60.0, 60.0)
- added K2: EA2-12NU, Audio-DSP:EA2-12NU, F.Cu at (71.7, 60.0)
- added Q1: BC847, Package_TO_SOT_SMD:SOT-23, B.Cu at (81.9, 69.0)
- added Q2: BC847, Package_TO_SOT_SMD:SOT-23, B.Cu at (82.0, 76.0)
- added R126: 1k, Resistor_SMD:R_0805_2012Metric, F.Cu at (339.2, 25.6)
- added R127: 1k, Resistor_SMD:R_0805_2012Metric, F.Cu at (339.2, 28.6)
- added R128: 1k, Resistor_SMD:R_0402_1005Metric, F.Cu at (73.2, 69.1)
- added R129: 1k, Resistor_SMD:R_0402_1005Metric, F.Cu at (73.2, 71.1)
- added R130: 10R, Resistor_SMD:R_0805_2012Metric, F.Cu at (339.2, 31.5)
- added R131: 10R, Resistor_SMD:R_0805_2012Metric, F.Cu at (339.2, 34.5)
- added R132: 10R, Resistor_SMD:R_0805_2012Metric, F.Cu at (339.2, 37.4)
- added R133: 10R, Resistor_SMD:R_0805_2012Metric, F.Cu at (339.2, 40.4)
- added R134: 1k, Resistor_SMD:R_0402_1005Metric, F.Cu at (73.2, 73.1)
- added R135: 1k, Resistor_SMD:R_0402_1005Metric, F.Cu at (73.2, 75.1)
- added U34: TL072, Package_SO:SOIC-8_3.9x4.9mm_P1.27mm, F.Cu at (58.4, 71.4)
- added U35: TL072, Package_SO:SOIC-8_3.9x4.9mm_P1.27mm, F.Cu at (58.4, 77.8)
- J15: value Conn_01x02 -> Conn_01x04; footprint Connector_Phoenix_MC:PhoenixContact_MCV_1,5_2-G-3.5_1x02_P3.50mm_Vertical -> Connector_PinHeader_2.54mm:PinHeader_1x04_P2.54mm_Vertical
- moved U10 240.9 mm to (97.0, 135.0)
- moved RN6 50.3 mm to (373.7, 120.0)
- moved RN5 50.3 mm to (370.7, 120.0)
- moved C105 46.0 mm to (343.7, 37.7)
- moved C106 46.0 mm to (343.7, 40.7)
- moved C107 46.0 mm to (343.7, 43.7)
- moved C108 46.0 mm to (343.7, 46.7)
- moved C35 46.0 mm to (343.7, 25.6)
- moved C40 46.0 mm to (343.7, 28.7)
- moved C41 46.0 mm to (343.7, 31.7)
- moved C90 46.0 mm to (343.7, 34.7)
- moved U25 36.0 mm to (347.7, 57.5)
- moved U5 36.0 mm to (347.7, 53.0)
- moved C110 32.2 mm to (363.2, 48.7)
- moved C115 32.2 mm to (378.1, 45.0)
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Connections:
- net /POWER_SUPPLIES/UI_POWER renamed +5VD1
- C105 pad 2: /ADC_CH1_2/RCA_JACK_CH1(REF) -> Net-(D4-A1)
- C90 pad 2: /ADC_CH1_2/RCA_JACK_CH1(REF) -> Net-(D3-A1)
- J14 pad 1: +12VD1 -> /FPGA_POWER
- J2 pad 1: unconnected-(J2-Pin_1-Pad1) -> /ADC_CH3_4/XLR_CH4(+)
- J2 pad 3: unconnected-(J2-Pin_3-Pad3) -> /ADC_CH3_4/XLR_CH4(-)
- J3 pad 1: /ADC_CH1_2/RCA_JACK_CH1(+) -> /ADC_CH1_2/RCA_CH1(+)
- J3 pad 2: /ADC_CH1_2/RCA_JACK_CH1(REF) -> /ADC_CH1_2/RCA_CH1(REF)
- J4 pad 1: /ADC_CH1_2/RCA_JACK_CH2(+) -> /ADC_CH1_2/JACK_CH1(+)
- J4 pad 2: /ADC_CH1_2/RCA_JACK_CH2(REF) -> /ADC_CH1_2/JACK_CH1(REF)
- NT3 pad 2: /ADC_CH1_2/RCA_JACK_CH1(REF) -> Net-(D3-A1)
- NT4 pad 2: /ADC_CH1_2/RCA_JACK_CH1(REF) -> Net-(D4-A1)
- R104 pad 1: /ADC_CH1_2/RCA_JACK_CH1(+) -> Net-(K2-Pad3)
- R104 pad 2: /ADC_CH1_2/RCA_JACK_CH1(REF) -> Net-(D4-A1)
- R105 pad 1: /ADC_CH1_2/RCA_JACK_CH1(+) -> Net-(K2-Pad3)
- R107 pad 1: /ADC_CH1_2/RCA_JACK_CH1(REF) -> Net-(D4-A1)
- R40 pad 1: /ADC_CH1_2/RCA_JACK_CH1(REF) -> Net-(D3-A1)
- R49 pad 1: /ADC_CH1_2/RCA_JACK_CH1(+) -> Net-(K1-Pad3)
- R86 pad 1: /ADC_CH1_2/RCA_JACK_CH1(+) -> Net-(K1-Pad3)
- R86 pad 2: /ADC_CH1_2/RCA_JACK_CH1(REF) -> Net-(D3-A1)

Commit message: Worked on main board
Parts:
- added J18: Conn_01x05, Connector_JST:JST_XH_B5B-XH-A_1x05_P2.50mm_Vertical, F.Cu at (102.0, 222.0)
- added J19: Conn_01x05, Connector_JST:JST_XH_B5B-XH-A_1x05_P2.50mm_Vertical, F.Cu at (109.8, 222.0)
- added J20: Conn_01x05, Connector_JST:JST_XH_B5B-XH-A_1x05_P2.50mm_Vertical, F.Cu at (117.6, 222.0)
- added J21: Conn_01x05, Connector_JST:JST_XH_B5B-XH-A_1x05_P2.50mm_Vertical, F.Cu at (125.4, 222.0)
- J15: value Conn_01x04 -> Conn_01x06; footprint Connector_PinHeader_2.54mm:PinHeader_1x04_P2.54mm_Vertical -> Connector_JST:JST_PH_B6B-PH-K_1x06_P2.00mm_Vertical
- moved J15 297.1 mm to (64.5, 222.0), turned to 90 degrees
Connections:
- J15 pad 1: unconnected-(J15-Pin_1-Pad1) -> GND
- J15 pad 3: unconnected-(J15-Pin_3-Pad3) -> +5VD1
- J15 pad 4: unconnected-(J15-Pin_4-Pad4) -> /FPGA/UI_TX

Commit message: Worked on main board
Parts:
- moved R1 0.07 mm to (330.4, 67.0)
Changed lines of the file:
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@@
   )
   (footprint "Resistor_SMD:R_0805_2012Metric" (layer "F.Cu")
-    (at 330.45 67.07)
+    (at 330.45 67)
     (descr "Resistor SMD 0805 (2012 Metric), square (rectangular) end terminal, IPC_7351 nominal, (Body size source: IPC-SM-782 page 72, https://www.pcb-3d.com/wordpress/wp-content/uploads/ipc-sm-782a_amendment_1_and_2.pdf), generated with kicad-footprint-generator")
     (tags "resistor")
